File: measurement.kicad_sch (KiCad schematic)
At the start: 22 parts, among them U1501 TLV9352, U1502 ACS730xLCTR-20AB

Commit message: edit trimmer adjustment style to sideways
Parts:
- RV1501: footprint pss:Potentiometer_Bourns_PVG5A -> pss:Potentiometer_Bourns_PVG5H; MPN PVG5A102C03B00 -> PVG5H102C03R00; VPN 81-PVG5A102C03B00 -> 81-PVG5H102C03R00
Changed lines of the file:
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@@
 		(title "Power Supply Sink")
 		(date "2024-12-07")
-		(rev "0.13.3")
+		(rev "0.13.4")
 		(company "Open Battery Tester")
 		(comment 1 "Measurement")
@@
 			)
 		)
-		(property "Footprint" "pss:Potentiometer_Bourns_PVG5A"
+		(property "Footprint" "pss:Potentiometer_Bourns_PVG5H"
 			(at 101.6 168.91 0)
 			(effects
@@
 			)
 		)
-		(property "MPN" "PVG5A102C03B00"
+		(property "MPN" "PVG5H102C03R00"
 			(at 101.6 168.91 0)
 			(effects
@@
 			)
 		)
-		(property "VPN" "81-PVG5A102C03B00"
+		(property "VPN" "81-PVG5H102C03R00"
 			(at 101.6 168.91 0)
 			(effects

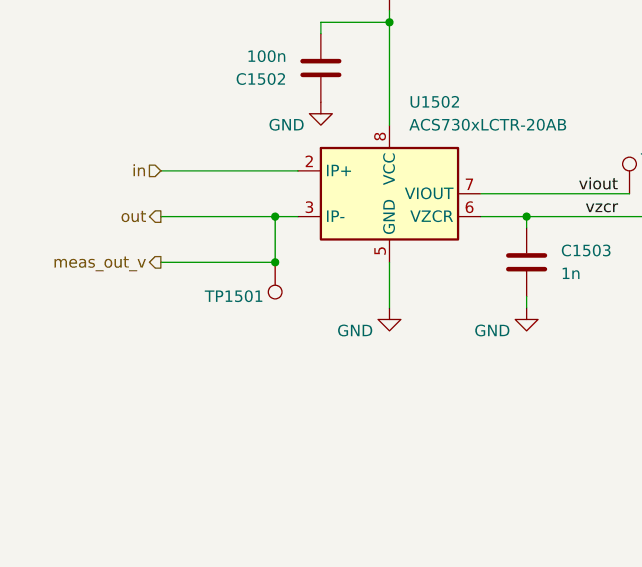
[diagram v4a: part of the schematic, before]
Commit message: remove measurement duplicate testpoint
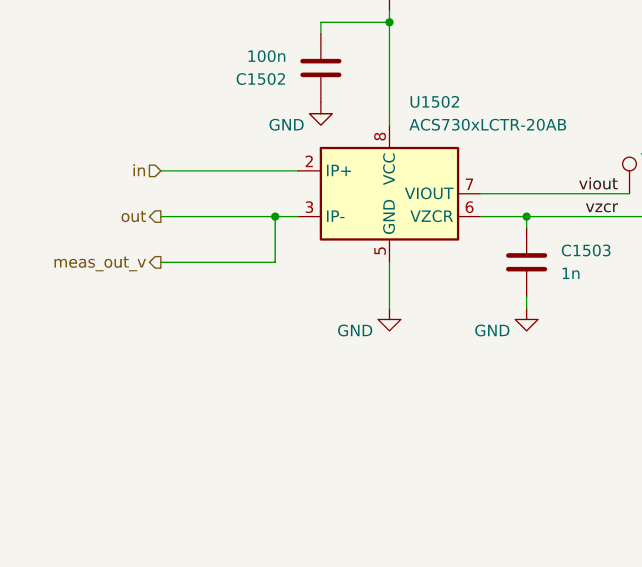
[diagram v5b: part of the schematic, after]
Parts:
- removed TP1501: ~, pss:TP_0805_2012Metric, symbol pss:TestPoint
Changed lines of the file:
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@@
 		(title "Power Supply Sink")
 		(date "2024-12-09")
-		(rev "0.13.7")
+		(rev "0.13.8")
 		(company "Open Battery Tester")
 		(comment 1 "Measurement")
@@
 	(junction
 		(at 246.38 87.63)
-		(diameter 0)
-		(color 0 0 0 0)
-	)
-	(junction
-		(at 63.5 100.33)
 		(diameter 0)
 		(color 0 0 0 0)
@@
 					(unit 1)
 				)
-			)
-		)
-	)
-	(symbol
-		(lib_id "pss:TestPoint")
-		(at 63.5 100.33 180)
-		(unit 1)
-		(exclude_from_sim no)
-		(in_bom yes)
-		(on_board yes)
-		(dnp no)
-		(property "Reference" "TP1501"
-			(at 62.23 104.14 0)
-			(effects
-				(font
-					(size 1.27 1.27)
-				)
-				(justify left)
-			)
-		)
-		(property "Value" "~"
-			(at 60.96 102.3621 0)
-			(effects
-				(font
-					(size 1.27 1.27)
-				)
-				(justify left)
-			)
-		)
-		(property "Footprint" "pss:TP_0805_2012Metric"
-			(at 58.42 100.33 0)
-			(effects
-				(font
-					(size 1.27 1.27)
-				)
-				(hide yes)
-			)
-		)
-		(property "Datasheet" "./datasheet/RCTCTE.pdf"
-			(at 58.42 100.33 0)
-			(effects
-				(font
-					(size 1.27 1.27)
-				)
-				(hide yes)
-			)
-		)
-		(property "Description" "test point"
-			(at 63.5 100.33 0)
-			(effects
-				(font
-					(size 1.27 1.27)
-				)
-				(hide yes)
-			)
-		)
-		(property "MPN" "RCTCTE"
-			(at 63.5 100.33 0)
-			(effects
-				(font
-					(size 1.27 1.27)
-				)
-				(hide yes)
-			)
-		)
-		(property "VPN" "660-RCTCTE"
-			(at 63.5 100.33 0)
-			(effects
-				(font
-					(size 1.27 1.27)
-				)
-				(hide yes)
-			)
-		)
-		(pin "1"
-		)
-		(instances
-			(project "pss"
-				(path "/3c438cf7-9350-4e9f-8115-1deba8984176/930a3603-b5c1-4234-96f5-716c518f6fe1"
-					(reference "TP1501")
-					(unit 1)
-				)
